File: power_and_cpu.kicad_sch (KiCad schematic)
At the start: 62 parts, among them J1 USB_C_Receptacle_USB2.0, J2 Conn_01x05, J3 Conn_01x06, J4 Conn_01x04, J5 Conn_01x04, J6 Conn_01x03, SW1 SW_MEC_5G, U11 RP2040, U13 ADC081S021CISD/NOPB, U6 NCP1117-3.3_SOT223, U7 XL7045, U9 W25Q128JVS, Y1 Crystal_GND24

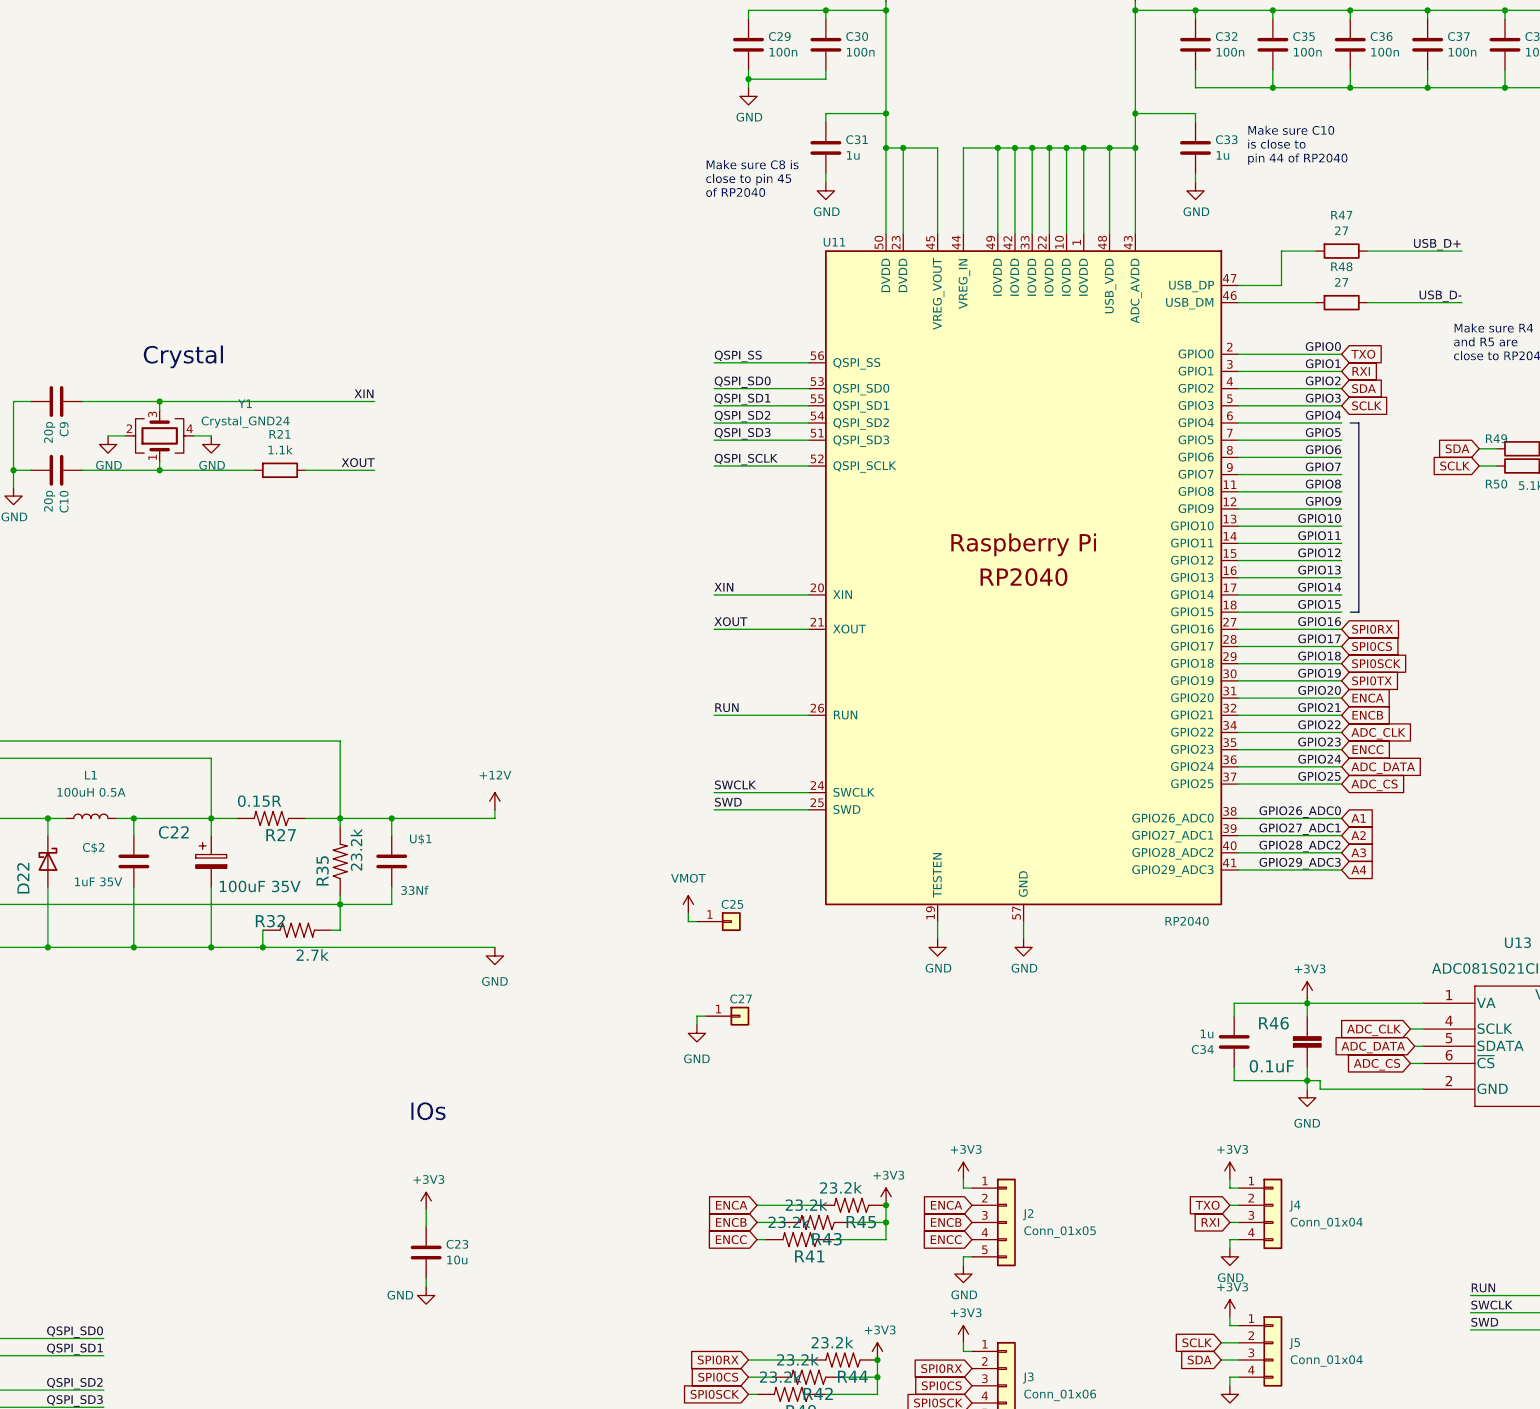
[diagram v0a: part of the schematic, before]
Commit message: Updated design rules and fixed routing to eliminate all copper DRC errors.
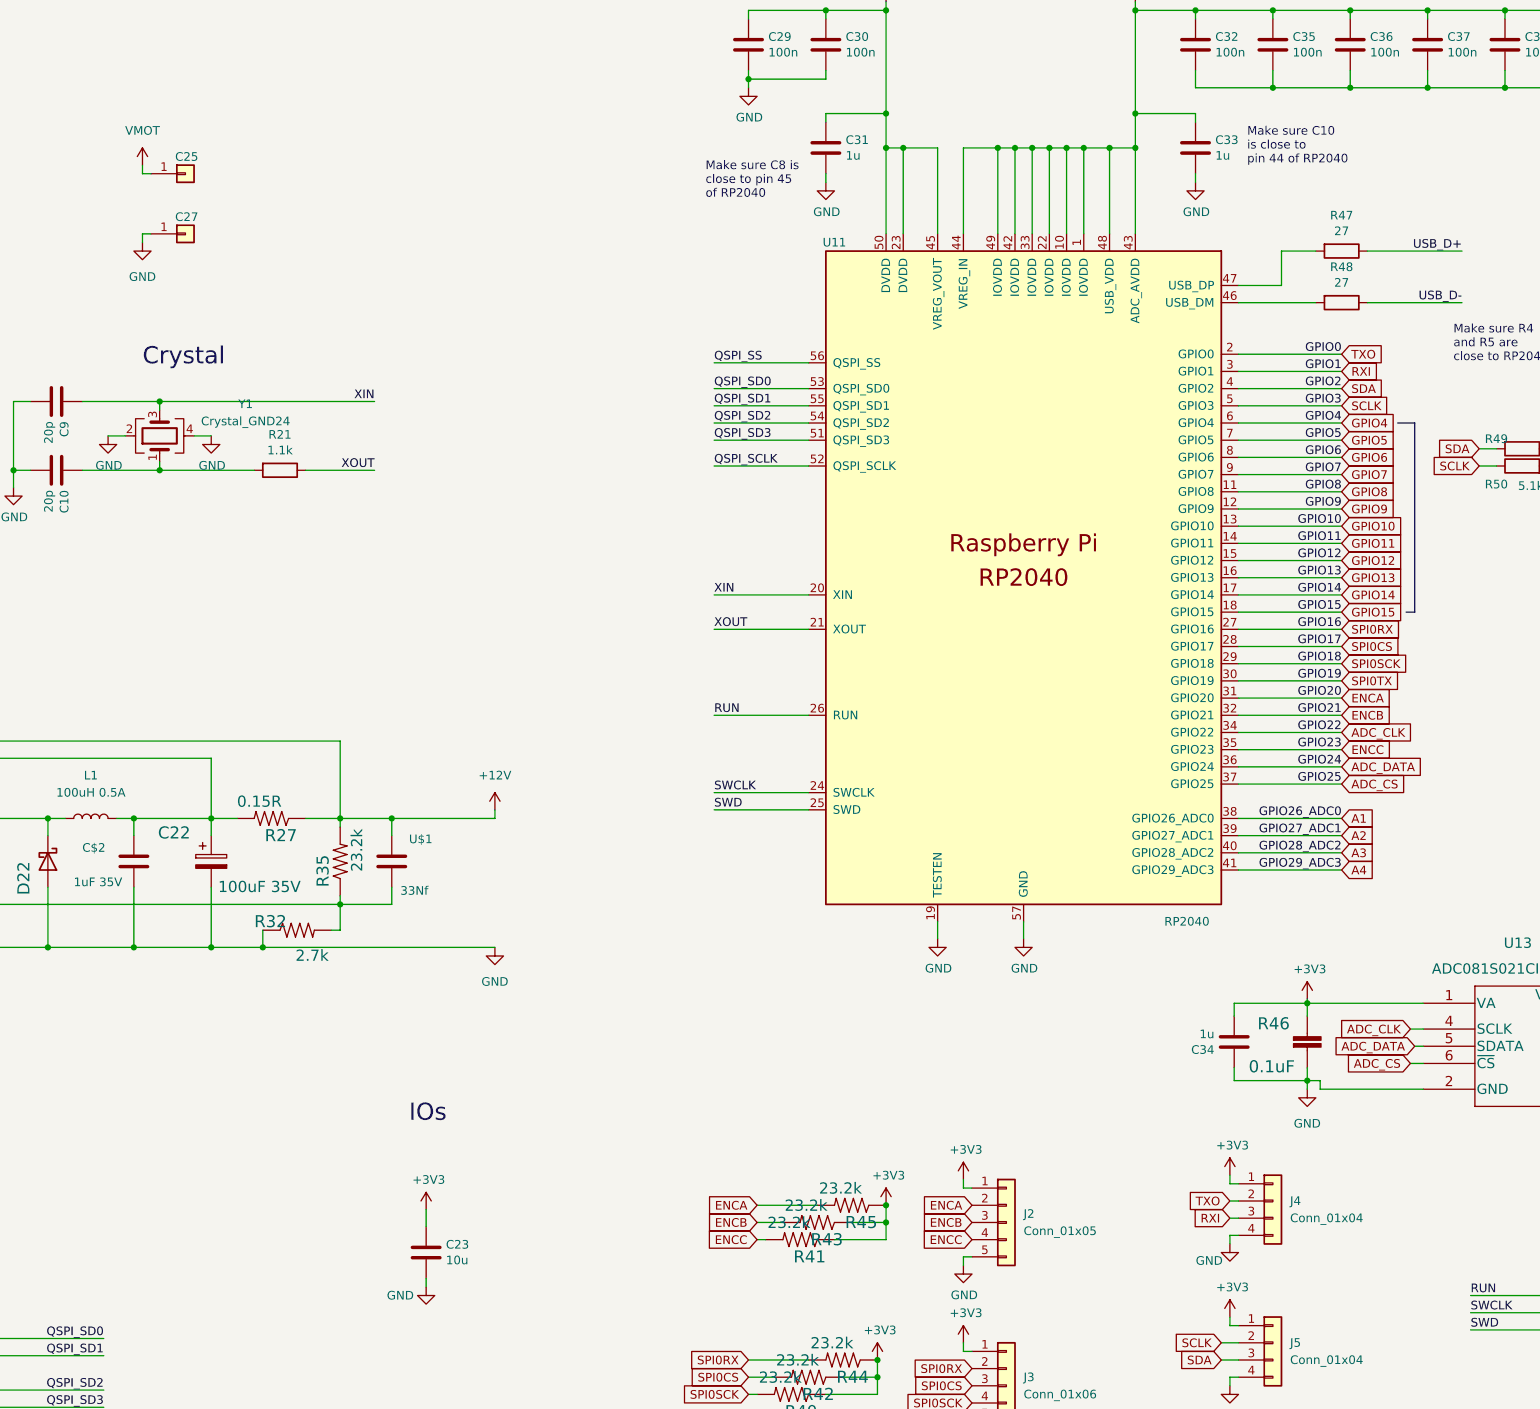
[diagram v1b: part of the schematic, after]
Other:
- moved on the sheet: C25, C27, J4

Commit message: I think layout is complete and the board is ready to order.
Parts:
- added D34, D35, D36: WS2812B, RP2040_minimal:LED_WS2812_3528_3.5x2.8mm_P1.5mm, symbol MotorBuck:WS2812B
- added JP1: SolderJumper_2_Open, Jumper:SolderJumper-2_P1.3mm_Open_RoundedPad1.0x1.5mm, symbol Jumper:SolderJumper_2_Open
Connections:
- net +3V3: now also D34.3 (VDD), D35.3 (VDD), D36.3 (VDD)
- net GND: now also D34.1 (GND), D35.1 (GND), D36.1 (GND)
- net SPI0TX: now also JP1.1 (A)
- new net: D34.2 (DIN), JP1.2 (B)
- new net: D34.4 (DOUT), D35.2 (DIN)
- new net: D35.4 (DOUT), D36.2 (DIN)

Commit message: Small updates to copper and silk
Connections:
- net USB_DN: now reaches R48.2, U11.46 (USB_DM)
- net USB_DP: now reaches R47.2, U11.47 (USB_DP)
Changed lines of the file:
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@@
     (effects (font (size 1.27 1.27)) (justify right bottom))
+  )
+  (label "USB_DN" (at 309.88 81.28 0)
+    (effects (font (size 1.27 1.27)) (justify left bottom))
   )
   (label "SWD" (at 341.63 233.045 0)
@@
     (effects (font (size 1.27 1.27)) (justify right bottom))
   )
+  (label "USB_DP" (at 313.69 75.565 90)
+    (effects (font (size 1.27 1.27)) (justify left bottom))
+  )
   (label "QSPI_SS" (at 229.87 90.17 0)

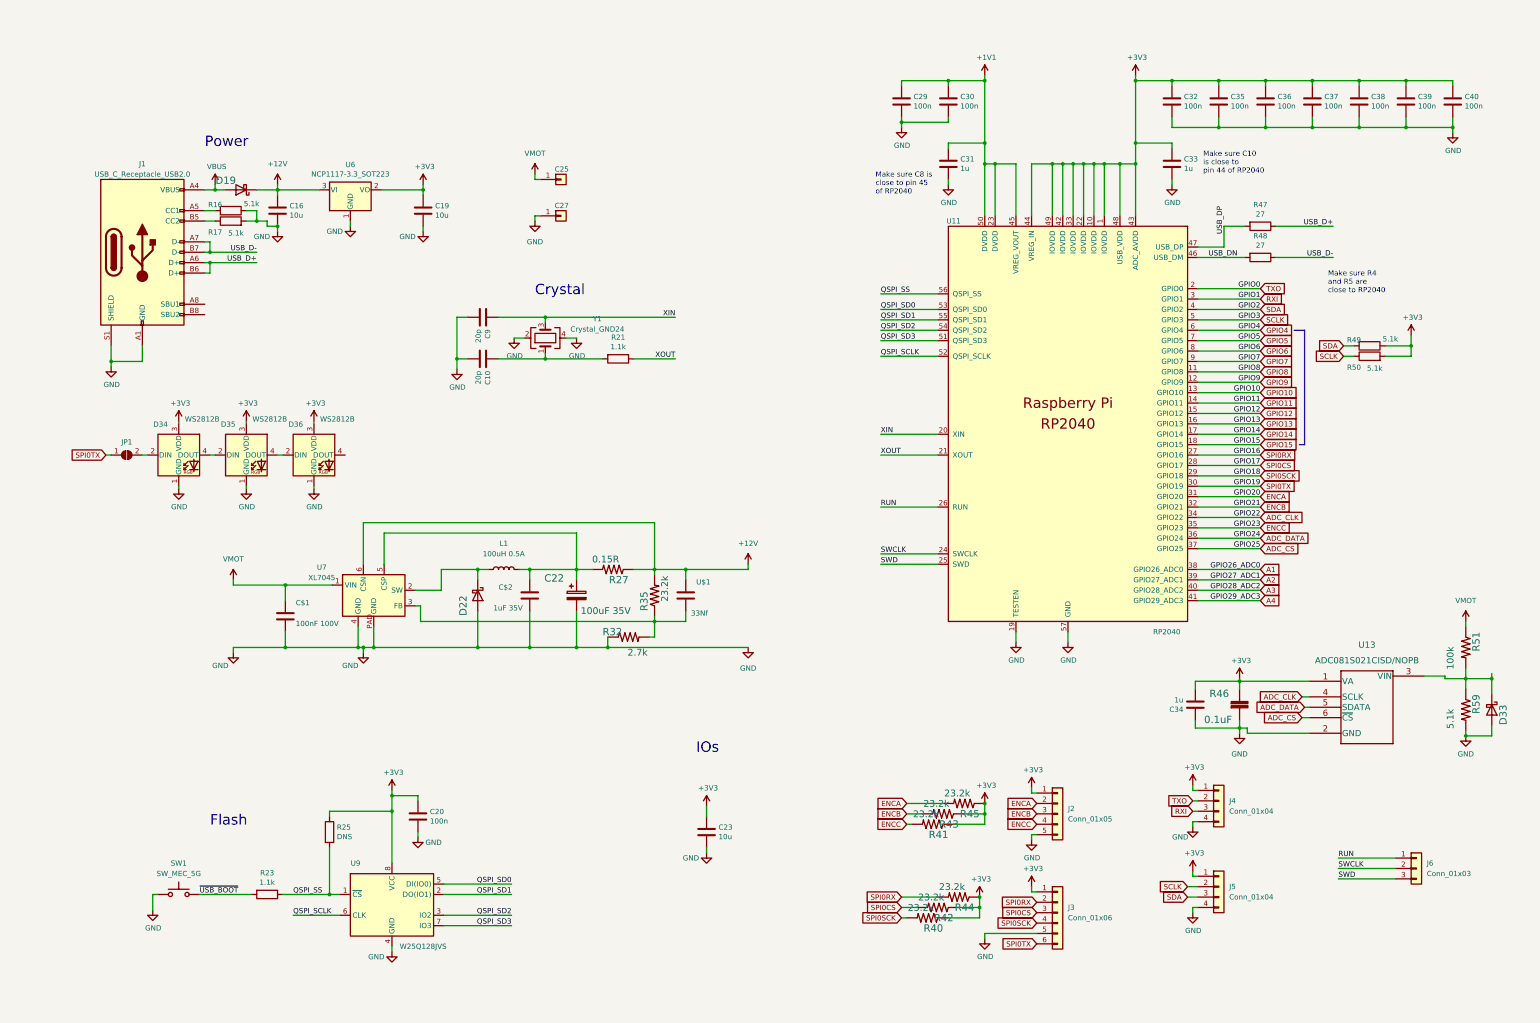
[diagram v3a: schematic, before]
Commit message: Updated PCB design based on feedback. Added thermistors, mounting holes. This design has better current carrying capacity. gerber folder may not be perfect right now.
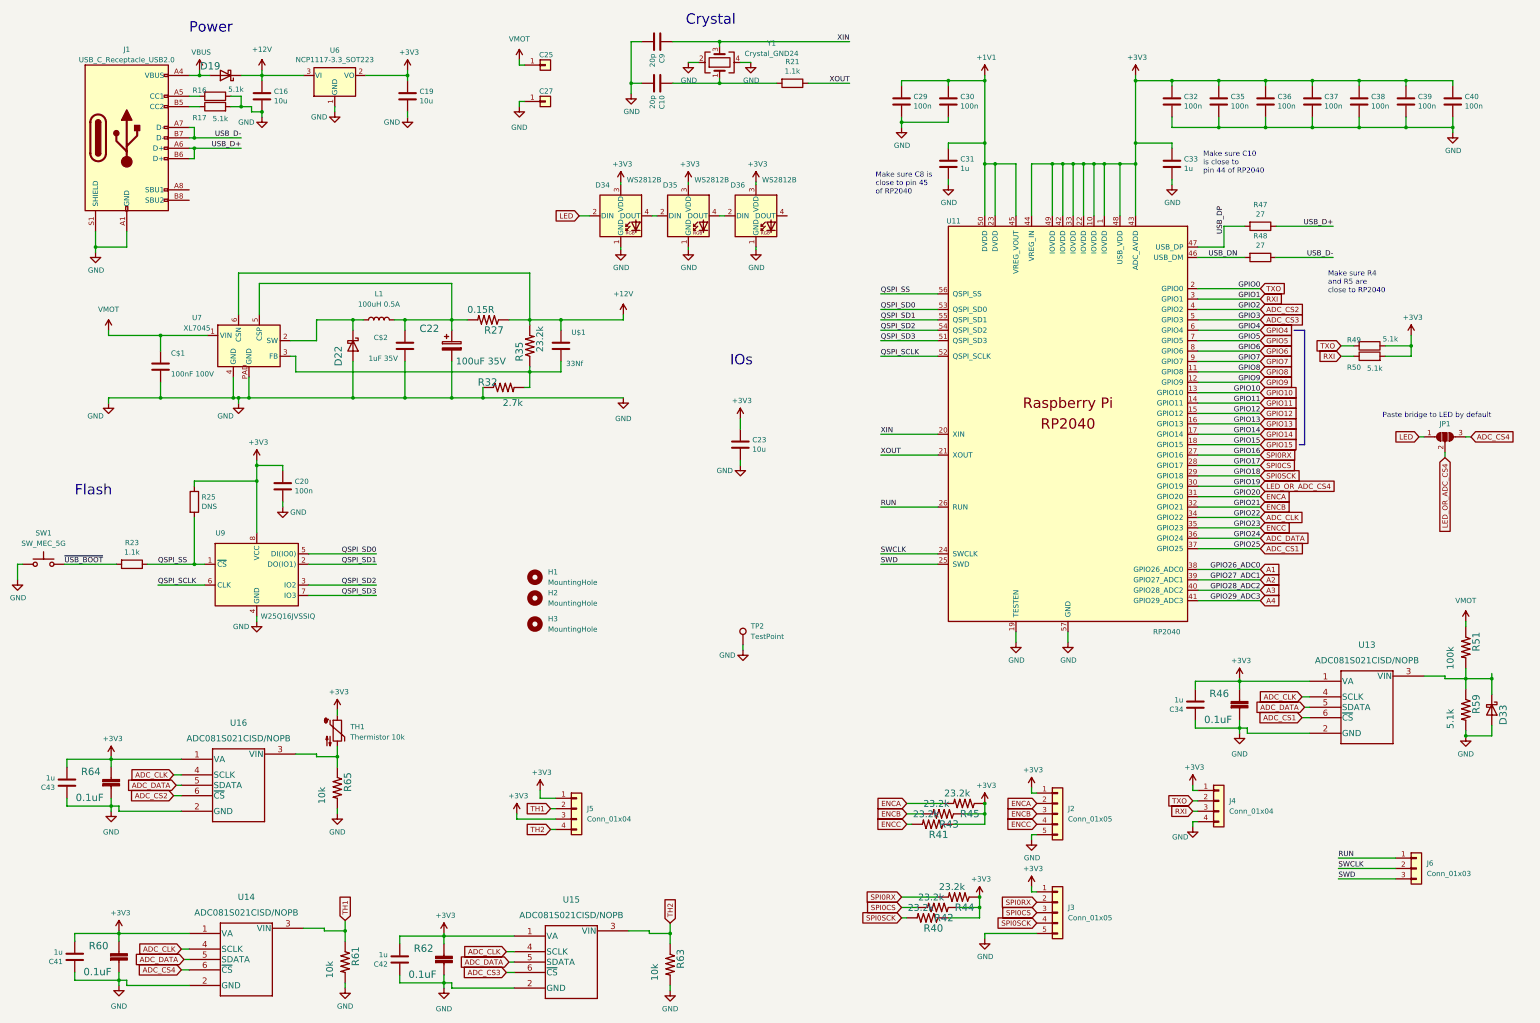
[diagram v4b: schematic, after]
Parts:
- removed J3: Conn_01x06, Connector_Molex:Molex_KK-254_AE-6410-06A_1x06_P2.54mm_Vertical, symbol Connector_Generic:Conn_01x06
- removed JP1: SolderJumper_2_Open, Jumper:SolderJumper-2_P1.3mm_Open_RoundedPad1.0x1.5mm, symbol Jumper:SolderJumper_2_Open
- added C41, C42, C43: 1u, Capacitor_SMD:C_0603_1608Metric, symbol Device:C
- added H1, H2, H3: MountingHole, RP2040_minimal:MountingHole_3.9mm_Plastite_#6, symbol Mechanical:MountingHole
- added J3: Conn_01x05, Connector_Molex:Molex_KK-254_AE-6410-05A_1x05_P2.54mm_Vertical, symbol Connector_Generic:Conn_01x05
- added JP1: SolderJumper_3_Open, Jumper:SolderJumper-3_P1.3mm_Open_RoundedPad1.0x1.5mm_NumberLabels, symbol Jumper:SolderJumper_3_Open
- added R60, R62, R64: 0.1uF, Capacitor_SMD:C_0603_1608Metric, symbol MotorController:SPARKFUN-CAPACITORS_CAP
- added R61, R63, R65: 10k, Resistor_SMD:R_0603_1608Metric, symbol MotorController:TAYLOR_RESISTOR
- added TH1: Thermistor 10k, Resistor_SMD:R_0603_1608Metric, symbol Device:Thermistor_NTC
- added TP2: TestPoint, TestPoint:TestPoint_Keystone_5019_Minature, symbol Connector:TestPoint
- added U14, U15, U16: ADC081S021CISD/NOPB, Package_TO_SOT_SMD:SOT-23-6, symbol 2022-06-16_01-48-54:ADC081S021CISD/NOPB
- U13: footprint ADC081S021:ADC081S021CISD&slash_NOPB -> Package_TO_SOT_SMD:SOT-23-6; LCSC (none) -> C130227
- U9: value W25Q128JVS -> W25Q16JVSSIQ; LCSC C97521 -> C82317
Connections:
- net +3V3: now also J5.3 (Pin_3), C41.2, C42.2, C43.2, J3.1 (Pin_1), R60.1, R62.1, R64.1, TH1.1, U14.1 (VA), U15.1 (VA), U16.1 (VA)
- net ADC_CLK: now also U14.4 (SCLK), U15.4 (SCLK), U16.4 (SCLK)
- net ADC_DATA: now also U14.5 (SDATA), U15.5 (SDATA), U16.5 (SDATA)
- net GND: now also C41.1, C42.1, C43.1, J3.5 (Pin_5), R60.2, R61.2, R62.2, R63.2, R64.2, R65.2, TP2.1, U14.2 (GND), U15.2 (GND), U16.2 (GND); no longer J5.4 (Pin_4)
- net RXI: now also R50.1
- net SPI0CS: now also J3.3 (Pin_3)
- net SPI0RX: now also J3.2 (Pin_2)
- net SPI0SCK: now also J3.4 (Pin_4)
- net TXO: now also R49.2
- net LED: now reaches D34.2 (DIN)
- net LED: now also JP1.1 (A)
- net ADC_CS renamed ADC_CS1
- removed net SCLK: J5.2 (Pin_2), R50.1, U11.5 (GPIO3)
- removed net SDA: J5.3 (Pin_3), R49.2, U11.4 (GPIO2)
- net SPI0TX renamed LED_OR_ADC_CS4
- net LED_OR_ADC_CS4: now also JP1.2 (C)
- new net: R65.1, TH1.2, U16.3 (VIN)
- new net ADC_CS2: U11.4 (GPIO2), U16.6 (~{CS})
- new net ADC_CS3: U11.5 (GPIO3), U15.6 (~{CS})
- new net ADC_CS4: JP1.3 (B), U14.6 (~{CS})
- new net TH1: J5.2 (Pin_2), R61.1, U14.3 (VIN)
- new net TH2: J5.4 (Pin_4), R63.1, U15.3 (VIN)
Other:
- note added: "Paste bridge to LED by default"
- moved on the sheet: C$1, C$2, C10, C16, C19, C20, C22, C23, C25, C27, C9, D19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
